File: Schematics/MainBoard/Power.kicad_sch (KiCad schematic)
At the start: 90 parts, among them IC2 MP2636GR-P, J2 USBPD_PROG, J3 USB_C_Receptacle_USB2.0_16P, J4 BATTERY JST PH-2A, Q1 STL9P3LLH6, Q3 STL9P3LLH6, U6 STUSB4500QTR, U7 AP63203WU

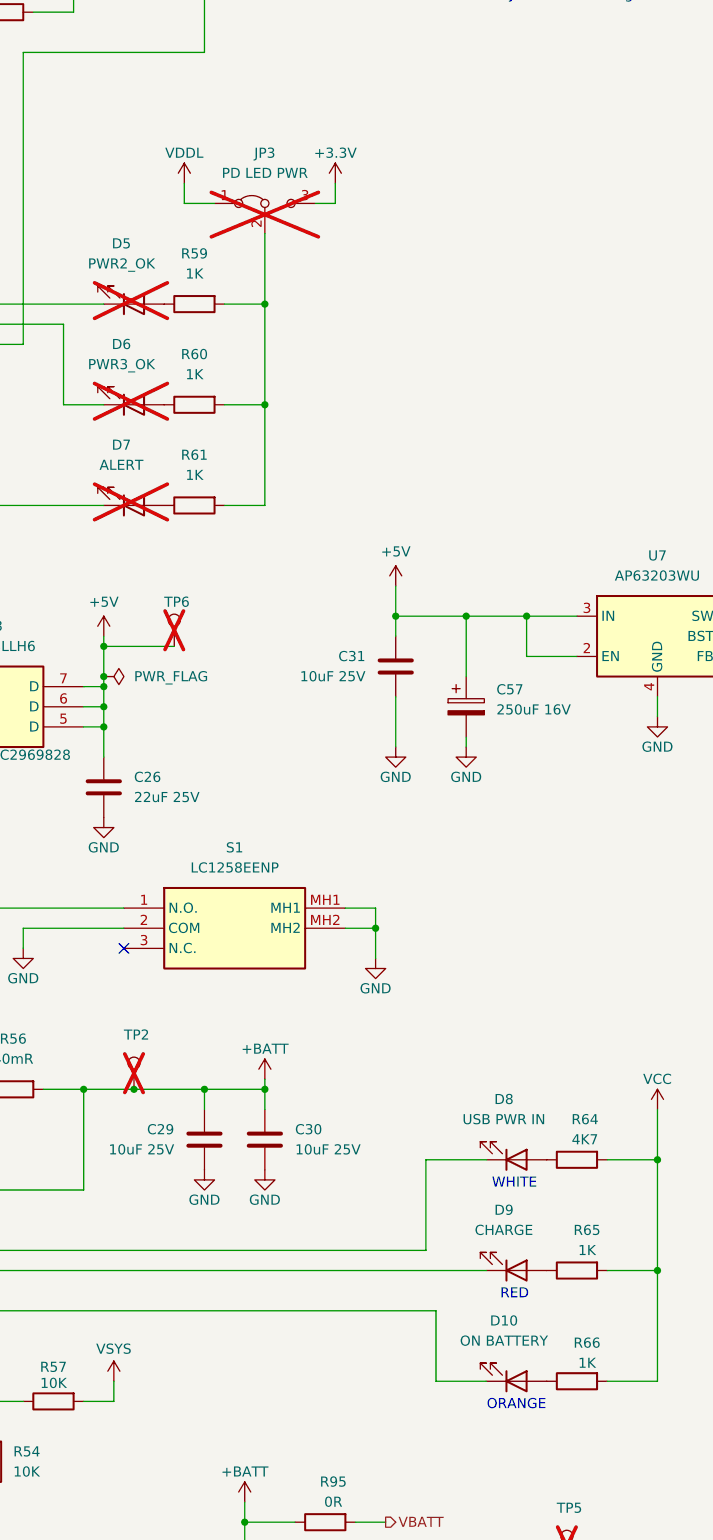
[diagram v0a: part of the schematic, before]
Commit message: Work on parts placement, remove excess LEDs
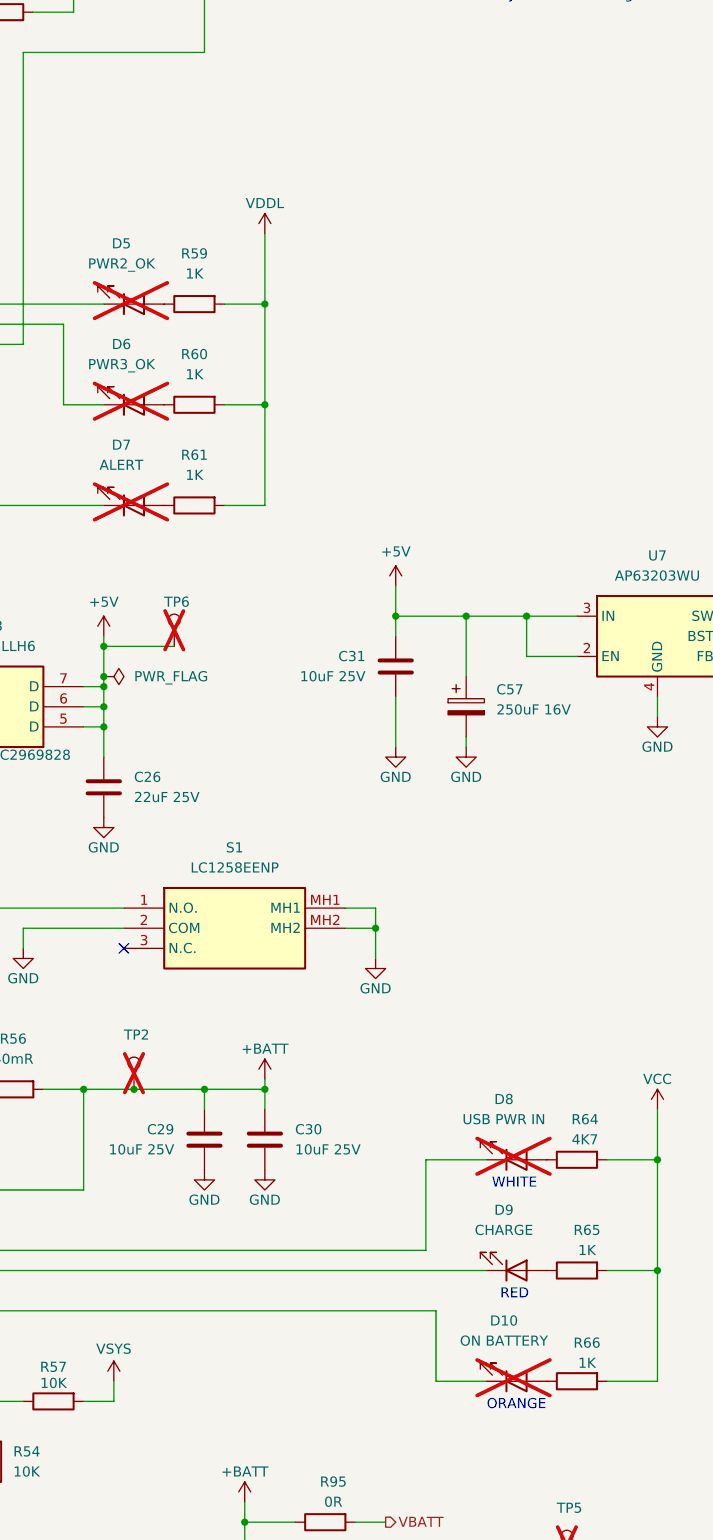
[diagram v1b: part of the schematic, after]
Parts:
- removed JP3: PD LED PWR, Jumpers:SolderJumper-3_P1.3mm_Bridged12_Pad1.0x1.5mm_NumberLabels, symbol Jumper:Jumper_3_Bridged12
- D10, D8: now not fitted
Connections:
- net VDDL: now also R59.2, R60.2, R61.2
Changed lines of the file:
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@@
 	(wire
 		(pts
-			(xy 264.16 64.77) (xy 264.16 67.31)
-		)
-		(stroke
-			(width 0)
-			(type default)
-		)
-	)
-	(wire
-		(pts
 			(xy 299.72 119.38) (xy 307.34 119.38)
 		)
@@
 	(wire
 		(pts
-			(xy 283.21 67.31) (xy 280.67 67.31)
-		)
-		(stroke
-			(width 0)
-			(type default)
-		)
-	)
-	(wire
-		(pts
 			(xy 137.16 209.55) (xy 144.78 209.55)
 		)
@@
 	(wire
 		(pts
-			(xy 264.16 67.31) (xy 267.97 67.31)
-		)
-		(stroke
-			(width 0)
-			(type default)
-		)
-	)
-	(wire
-		(pts
 			(xy 93.98 72.39) (xy 130.81 72.39)
 		)
@@
 	(wire
 		(pts
-			(xy 283.21 64.77) (xy 283.21 67.31)
-		)
-		(stroke
-			(width 0)
-			(type default)
-		)
-	)
-	(wire
-		(pts
 			(xy 313.69 124.46) (xy 307.34 124.46)
 		)
@@
 		(in_bom yes)
 		(on_board yes)
-		(dnp no)
+		(dnp yes)
 		(fields_autoplaced yes)
 		(property "Reference" "D10"
@@
 	(symbol
 		(lib_id "power:VDDF")
-		(at 264.16 64.77 0)
+		(at 274.32 71.12 0)
 		(unit 1)
 		(exclude_from_sim no)
@@
 		(dnp no)
 		(property "Reference" "#PWR0126"
-			(at 264.16 68.58 0)
+			(at 274.32 74.93 0)
 			(effects
 				(font
@@
 		)
 		(property "Value" "VDDL"
-			(at 264.16 60.96 0)
+			(at 274.32 67.31 0)
 			(effects
 				(font
@@
 		)
 		(property "Footprint" ""
-			(at 264.16 64.77 0)
+			(at 274.32 71.12 0)
 			(effects
 				(font
@@
 		)
 		(property "Datasheet" ""
-			(at 264.16 64.77 0)
+			(at 274.32 71.12 0)
 			(effects
 				(font
@@
 		)
 		(property "Description" "Power symbol creates a global label with name \"VDDF\""
-			(at 264.16 64.77 0)
+			(at 274.32 71.12 0)
 			(effects
 				(font
@@
 	)
 	(symbol
-		(lib_id "Jumper:Jumper_3_Bridged12")
-		(at 274.32 67.31 0)
-		(unit 1)
-		(exclude_from_sim no)
-		(in_bom no)
-		(on_board yes)
-		(dnp yes)
-		(fields_autoplaced yes)
-		(property "Reference" "JP3"
-			(at 274.32 60.96 0)
-			(effects
-				(font
-					(size 1.27 1.27)
-				)
-			)
-		)
-		(property "Value" "PD LED PWR"
-			(at 274.32 63.5 0)
-			(effects
-				(font
-					(size 1.27 1.27)
-				)
-			)
-		)
-		(property "Footprint" "Jumpers:SolderJumper-3_P1.3mm_Bridged12_Pad1.0x1.5mm_NumberLabels"
-			(at 274.32 67.31 0)
-			(effects
-				(font
-					(size 1.27 1.27)
-				)
-				(hide yes)
-			)
-		)
-		(property "Datasheet" "~"
-			(at 274.32 67.31 0)
-			(effects
-				(font
-					(size 1.27 1.27)
-				)
-				(hide yes)
-			)
-		)
-		(property "Description" "Jumper, 3-pole, pins 1+2 closed/bridged"
-			(at 274.32 67.31 0)
-			(effects
-				(font
-					(size 1.27 1.27)
-				)
-				(hide yes)
-			)
-		)
-		(property "LCSC" "DNF"
-			(at 274.32 67.31 0)
-			(effects
-				(font
-					(size 1.27 1.27)
-				)
-				(hide yes)
-			)
-		)
-		(pin "3"
-		)
-		(pin "2"
-		)
-		(pin "1"
-		)
-		(instances
-			(project "LT6502"
-				(path "/a2243a34-697c-4939-97f7-df548e421864/023ed7d3-fbe9-4017-a116-821cc1971589"
-					(reference "JP3")
-					(unit 1)
-				)
-			)
-		)
-	)
-	(symbol
 		(lib_id "Interface_USB:STUSB4500QTR")
 		(at 165.1 82.55 0)
@@
 	)
 	(symbol
-		(lib_id "power:+3.3V")
-		(at 283.21 64.77 0)
-		(unit 1)
-		(exclude_from_sim no)
-		(in_bom yes)
-		(on_board yes)
-		(dnp no)
-		(fields_autoplaced yes)
-		(property "Reference" "#PWR0129"
-			(at 283.21 68.58 0)
-			(effects
-				(font
-					(size 1.27 1.27)
-				)
-				(hide yes)
-			)
-		)
-		(property "Value" "+3.3V"
-			(at 283.21 60.96 0)
-			(effects
-				(font
-					(size 1.27 1.27)
-				)
-			)
-		)
-		(property "Footprint" ""
-			(at 283.21 64.77 0)
-			(effects
-				(font
-					(size 1.27 1.27)
-				)
-				(hide yes)
-			)
-		)
-		(property "Datasheet" ""
-			(at 283.21 64.77 0)
-			(effects
-				(font
-					(size 1.27 1.27)
-				)
-				(hide yes)
-			)
-		)
-		(property "Description" ""
-			(at 283.21 64.77 0)
-			(effects
-				(font
-					(size 1.27 1.27)
-				)
-			)
-		)
-		(pin "1"
-		)
-		(instances
-			(project "LT6502"
-				(path "/a2243a34-697c-4939-97f7-df548e421864/023ed7d3-fbe9-4017-a116-821cc1971589"
-					(reference "#PWR0129")
-					(unit 1)
-				)
-			)
-		)
-	)
-	(symbol
 		(lib_id "Device:C_Small")
 		(at 250.19 36.83 0)
@@
 		(in_bom yes)
 		(on_board yes)
-		(dnp no)
+		(dnp yes)
 		(fields_autoplaced yes)
 		(property "Reference" "D8"

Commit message: Work on PCB
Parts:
- removed D7: ALERT, LED_SMD:LED_0603_1608Metric, symbol Device:LED
- removed D8: USB PWR IN, LED_SMD:LED_0805_2012Metric, symbol Device:LED
- removed R61: 1K, Resistor_SMD:R_0402_1005Metric, symbol Device:R
- removed R64: 4K7, Resistor_SMD:R_0402_1005Metric, symbol Device:R
- C15, C18: footprint Capacitor_SMD:C_0603_1608Metric -> Capacitor_SMD:C_0402_1005Metric
- C28: value 0.1uF -> 100nF; footprint Capacitor_SMD:C_0603_1608Metric -> Capacitor_SMD:C_0402_1005Metric
- C57, C58: value 250uF 16V -> 100uF 10V Tant; footprint Capacitor_SMD:CP_Elec_10x12.5 -> Capacitor_Tantalum_SMD:CP_EIA-7343-30_AVX-N; LCSC DNF -> DNP; Mouser Part Number 667-EEV-FK1V681Q -> (none)
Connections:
- net nALERT: no longer names the net of U6.19 (ALERT)
- no-connect marks 6 -> 8
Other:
- note removed: "WHITE"

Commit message: Completed routing
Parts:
- R33, R53: footprint Resistor_SMD:R_0402_1005Metric -> Resistor_SMD:R_0603_1608Metric
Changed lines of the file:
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@@
 			)
 		)
-		(property "Footprint" "Resistor_SMD:R_0402_1005Metric"
+		(property "Footprint" "Resistor_SMD:R_0603_1608Metric"
 			(at 110.998 52.07 90)
 			(effects
@@
 			)
 		)
-		(property "Footprint" "Resistor_SMD:R_0402_1005Metric"
+		(property "Footprint" "Resistor_SMD:R_0603_1608Metric"
 			(at 234.188 53.34 90)
 			(effects

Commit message: Updates based on production files for JLC
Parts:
- C15, C18, C28: LCSC C113803 -> C307331
- C57, C58: LCSC DNP -> C49332976
- D18: LCSC DNF -> C2296
- D9: LCSC DNF -> C84256
- J2, J3, J4, L1, S1: now not fitted
- L2: LCSC DNF -> C2762047
- R33: LCSC C11702 -> C21190
- R34, R38: LCSC C25905 -> DNF
- R46: LCSC ??? -> C25756
- R47: LCSC ??? -> C25750
- R48: LCSC (none) -> C2933084
- R84: LCSC (none) -> C25917
- R95: LCSC (none) -> DNF; now not fitted
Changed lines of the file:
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@@
 			)
 		)
-		(property "LCSC" ""
+		(property "LCSC" "C25917"
 			(at 367.03 185.42 90)
 			(effects
@@
 		(in_bom yes)
 		(on_board yes)
-		(dnp no)
+		(dnp yes)
 		(property "Reference" "J4"
 			(at 283.21 250.444 0)
@@
 		(in_bom yes)
 		(on_board yes)
-		(dnp no)
+		(dnp yes)
 		(property "Reference" "R95"
 			(at 282.956 228.6 90)
@@
 			)
 		)
-		(property "LCSC" ""
+		(property "LCSC" "DNF"
 			(at 281.94 233.68 90)
 			(effects
@@
 			)
 		)
-		(property "LCSC" "C113803"
+		(property "LCSC" "C307331"
 			(at 44.45 87.63 0)
 			(effects
@@
 		(in_bom yes)
 		(on_board yes)
-		(dnp no)
+		(dnp yes)
 		(fields_autoplaced yes)
 		(property "Reference" "L1"
@@
 			)
 		)
-		(property "LCSC" "C25905"
+		(property "LCSC" "DNF"
 			(at 123.19 111.76 0)
 			(effects
@@
 			)
 		)
-		(property "LCSC" "DNF"
+		(property "LCSC" "C84256"
 			(at 306.07 201.93 0)
 			(effects
@@
 			)
 		)
-		(property "LCSC" "???"
+		(property "LCSC" "C25756"
 			(at 160.02 231.14 90)
 			(effects
@@
 			)
 		)
-		(property "LCSC" "DNF"
+		(property "LCSC" "C2296"
 			(at 359.41 185.42 0)
 			(effects
@@
 			)
 		)
-		(property "LCSC" ""
+		(property "LCSC" "C2933084"
 			(at 176.53 241.3 90)
 			(effects
@@
 			)
 		)
-		(property "LCSC" "???"
+		(property "LCSC" "C25750"
 			(at 168.91 236.22 90)
 			(effects
@@
 			)
 		)
-		(property "LCSC" "C113803"
+		(property "LCSC" "C307331"
 			(at 250.19 36.83 0)
 			(effects
@@
 			)
 		)
-		(property "LCSC" "DNP"
+		(property "LCSC" "C49332976"
 			(at 389.89 129.54 0)
 			(effects
@@
 			)
 		)
-		(property "LCSC" "C11702"
+		(property "LCSC" "C21190"
 			(at 109.22 52.07 0)
 			(effects
@@
 			)
 		)
-		(property "LCSC" "C25905"
+		(property "LCSC" "DNF"
 			(at 129.54 111.76 0)
 			(effects
@@
 		(in_bom yes)
 		(on_board yes)
-		(dnp no)
+		(dnp yes)
 		(property "Reference" "S1"
 			(at 270.51 148.59 0)
@@
 			)
 		)
-		(property "LCSC" "C113803"
+		(property "LCSC" "C307331"
 			(at 132.08 212.09 0)
 			(effects
@@
 		(in_bom yes)
 		(on_board yes)
-		(dnp no)
+		(dnp yes)
 		(fields_autoplaced yes)
 		(property "Reference" "J3"
@@
 			)
 		)
-		(property "LCSC" "DNP"
+		(property "LCSC" "C49332976"
 			(at 299.72 130.81 0)
 			(effects
@@
 		(in_bom yes)
 		(on_board yes)
-		(dnp no)
+		(dnp yes)
 		(fields_autoplaced yes)
 		(property "Reference" "J2"
@@
 			)
 		)
-		(property "LCSC" "DNF"
+		(property "LCSC" "C2762047"
 			(at 355.6 119.38 90)
 			(effects
